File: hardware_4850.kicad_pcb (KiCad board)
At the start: 2 copper layers, 238 parts, among them J1 +, J10 Enable, J11 CAN_IN, J12 CAN_OUT, J13 Debug, J14 I2C, J2 Display, J3 A, J4 HALL, J5 B, J6 MOT_AUX, J7 C, J8 GND, J9 CRANK, P1 SWD, Q1 IPT015N10N5, Q2 IPT015N10N5, Q3 IPT015N10N5, Q4 IPT015N10N5, Q5 IPT015N10N5, Q6 IPT015N10N5, U1 1EDN7550B, U10 LM5008, U11 XC6206P332MR, U12 XC6206P332MR, U13 LMR12010X, U14 STM32G473VCTx, U15 SN65HVD230, U2 INA240A2PWR, U3 1EDN7550B, U4 1EDN7550B, U5 INA240A2PWR, U6 1EDN7550B, U7 1EDN7550B, U8 INA240A2PWR, U9 1EDN7550B, Y1 8MHz

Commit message: started the layout
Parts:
- added N1: Housing, footprints:HaiLong-Case, F.Cu at (50.0, 50.0)
- C15, C16, C3, C35, C36, C37, C38, C39, C4, C40, C41, C42, C43, C44, R17, R26, R8, U2, U5, U8: moved to B.Cu
- moved C44 253.2 mm to (87.5, 138.0), turned to 270 degrees
- moved C43 250.2 mm to (92.0, 138.0), turned to 270 degrees
- moved C10 249.1 mm to (55.4, 148.0)
- moved C11 249.1 mm to (46.0, 155.4)
- moved C12 249.1 mm to (31.9, 165.7)
- moved C5 249.1 mm to (51.7, 155.4)
- moved C6 249.1 mm to (43.6, 160.0)
- moved C7 249.1 mm to (61.1, 143.8)
- moved C8 249.1 mm to (38.0, 160.0)
- moved C9 249.1 mm to (37.5, 165.7)
- moved C40 246.9 mm to (105.5, 138.0), turned to 270 degrees
- moved C38 238.4 mm to (101.0, 133.0), turned to 90 degrees
- moved C47 237.2 mm to (11.7, 27.9)
- moved C48 237.2 mm to (5.95, 33.9)
- moved R29 237.2 mm to (14.5, 24.4)
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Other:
- board outline added: 100 x 55 mm
- board text added: "BATT Side"
- board text added: "Output Side"

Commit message: switched to old housing
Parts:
- removed J14: I2C, Connector_Wire:SolderWire-0.5sqmm_1x02_P4.6mm_D0.9mm_OD2.1mm
- added H1: MountingHole_Pad, MountingHole:MountingHole_3.2mm_M3_Pad_Via, F.Cu at (97.5, 94.5)
- added H2: MountingHole_Pad, MountingHole:MountingHole_3.2mm_M3_Pad_Via, F.Cu at (129.5, 94.5)
- added H3: MountingHole_Pad, MountingHole:MountingHole_3.2mm_M3_Pad_Via, F.Cu at (161.5, 94.5)
- C15, C16, C3, C35, C36, C37, C38, C39, C4, C40, C41, C42, C43, C44, R17, R26, R8, U2, U5, U8: moved to F.Cu
- J1, J3, J5, J7, J8: footprint Connector_Wire:SolderWire-2.5sqmm_1x01_D2.4mm_OD3.6mm -> footprints:8X8X8.4MM TERMINAL
- J10: footprint Connector_JST:JST_PH_S2B-PH-K_1x02_P2.00mm_Horizontal -> Connector_JST:JST_PH_B2B-PH-K_1x02_P2.00mm_Vertical
- J11, J12, J6, J9: footprint Connector_JST:JST_PH_S4B-PH-K_1x04_P2.00mm_Horizontal -> Connector_JST:JST_PH_B4B-PH-K_1x04_P2.00mm_Vertical
- J13: footprint Connector_USB:USB_Mini-B_Lumberg_2486_01_Horizontal -> Connector_USB:USB_Micro-B_Wuerth_614105150721_Vertical
- J2, J4: footprint Connector_JST:JST_PH_S5B-PH-K_1x05_P2.00mm_Horizontal -> Connector_JST:JST_PH_B5B-PH-K_1x05_P2.00mm_Vertical
- JP10, JP11, JP12, JP13, JP14, JP15, JP16, JP2, JP3, JP4, JP5, JP6, JP7, JP8, JP9: footprint Jumper:SolderJumper-2_P1.3mm_Bridged_RoundedPad1.0x1.5mm -> NetTie:NetTie-2_SMD_Pad0.5mm
- N1: footprint footprints:HaiLong-Case -> footprints:RND-455-00370
- moved C48 267.7 mm to (266.0, -29.6)
- moved C47 251.2 mm to (257.2, -25.0)
- moved U8 232.2 mm to (259.6, -28.5), turned to 0 degrees
- moved C16 228.1 mm to (249.2, -29.6)
- moved C15 217.5 mm to (240.5, -25.0)
- moved C32 187.0 mm to (249.2, -18.8)
- moved U5 183.3 mm to (242.9, -17.8), turned to 0 degrees
- moved C31 170.9 mm to (240.5, -14.3)
- moved U2 165.1 mm to (242.9, -28.5), turned to 0 degrees
- moved J1 133.0 mm to (175.5, 114.5), turned to 90 degrees
- moved U14 126.4 mm to (129.5, 66.5)
- moved R29 98.6 mm to (89.5, 88.5), turned to 90 degrees
- moved C12 97.3 mm to (117.0, 118.5), turned to 180 degrees
- moved C9 96.2 mm to (117.0, 111.5), turned to 180 degrees
- moved C8 86.6 mm to (112.0, 115.0)
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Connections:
- net /mcu/AIN_TEMP renamed /mcu/AIN_TEMP_A
- U14 pad 78: /mcu/I2C_SCL -> (no net)
- U14 pad 94: /mcu/I2C_SDA -> (no net)
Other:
- board size 100 x 55 mm -> 104 x 79 mm
- copper layers 2 -> 4
- board text removed: "BATT Side"
- board text removed: "Output Side"

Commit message: finished placing started layout
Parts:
- removed JP10: PBN+, NetTie:NetTie-2_SMD_Pad0.5mm
- removed JP12: PCN+, NetTie:NetTie-2_SMD_Pad0.5mm
- removed JP2: PA+, NetTie:NetTie-2_SMD_Pad0.5mm
- removed JP4: PB+, NetTie:NetTie-2_SMD_Pad0.5mm
- removed JP6: PC+, NetTie:NetTie-2_SMD_Pad0.5mm
- removed JP8: PAN+, NetTie:NetTie-2_SMD_Pad0.5mm
- added C92: 100n, Capacitor_SMD:C_0603_1608Metric, F.Cu at (132.6, 62.1)
- added C93: 100n, Capacitor_SMD:C_0603_1608Metric, F.Cu at (132.6, 68.2)
- added C94: 100n, Capacitor_SMD:C_0603_1608Metric, F.Cu at (109.1, 55.4)
- added C95: 100n, Capacitor_SMD:C_0603_1608Metric, F.Cu at (118.0, 55.4)
- added C96: 100n, Capacitor_SMD:C_0603_1608Metric, F.Cu at (106.2, 70.0)
- added R67: 10k, Resistor_SMD:R_0603_1608Metric, F.Cu at (112.1, 55.4)
- added R68: 1k, Resistor_SMD:R_0603_1608Metric, F.Cu at (132.6, 60.6)
- added R69: 33k, Resistor_SMD:R_0603_1608Metric, F.Cu at (140.7, 88.0)
- added R70: 10k, Resistor_SMD:R_0603_1608Metric, F.Cu at (132.6, 66.7)
- added R71: 1k, Resistor_SMD:R_0603_1608Metric, F.Cu at (110.6, 55.4)
- added R72: 33k, Resistor_SMD:R_0603_1608Metric, F.Cu at (107.8, 88.4)
- added R73: 10k, Resistor_SMD:R_0603_1608Metric, F.Cu at (119.5, 55.4)
- added R74: 1k, Resistor_SMD:R_0603_1608Metric, F.Cu at (106.2, 68.6)
- added TH2: NTC 10k, Resistor_SMD:R_0603_1608Metric, F.Cu at (134.0, 97.0)
- added TH3: NTC 10k, Resistor_SMD:R_0603_1608Metric, F.Cu at (166.5, 96.5)
- JP11, JP13, JP3, JP5, JP7, JP9: moved to B.Cu
- L2: value 4u7 -> 10u; footprint Inductor_SMD:L_1206_3216Metric -> Inductor_SMD:L_Taiyo-Yuden_NR-40xx
- R1: value 10k -> 33k
- R2: value 33k -> 1k
- R3: value 1k -> 33k
- moved J2 220.8 mm to (178.0, 87.5), turned to 90 degrees
- moved R3 204.7 mm to (173.2, 89.1), turned to 180 degrees
- moved R1 193.3 mm to (172.0, 86.0), turned to 180 degrees
- moved C48 187.8 mm to (102.5, 63.0), turned to 180 degrees
- moved U8 185.1 mm to (102.5, 69.4), turned to 90 degrees
- moved C47 178.7 mm to (102.5, 64.5), turned to 180 degrees
- moved R46 173.7 mm to (83.5, 89.2)
- moved J12 172.4 mm to (141.2, 72.0), turned to 0 degrees
- moved R47 167.7 mm to (83.5, 87.8)
- moved R48 161.8 mm to (83.5, 86.2)
- moved J11 161.6 mm to (141.2, 66.5), turned to 0 degrees
- moved D11 158.3 mm to (80.5, 87.8)
- moved JP13 156.2 mm to (116.4, 77.9), turned to 270 degrees
- moved C78 153.4 mm to (129.3, 74.4), turned to 270 degrees
- moved D10 150.3 mm to (80.5, 89.2)
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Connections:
- net Net-(C29-Pad2) renamed /phase_b/Phase-
- net Net-(C45-Pad2) renamed /phase_c/Phase-
- C1 pad 1: /mcu/AIN_TEMP_A -> /mcu/AIN_VDC
- C13 pad 2: Net-(C13-Pad2) -> /phase_a/Phase-
- C14 pad 2: Net-(C13-Pad2) -> /phase_a/Phase-
- C2 pad 1: /mcu/AIN_VDC -> /mcu/AIN_TEMP_A
- J3 pad 1: /phase_a/Phase -> Net-(J3-Pad1)
- J5 pad 1: /phase_b/Phase -> Net-(J5-Pad1)
- J7 pad 1: /phase_c/Phase -> Net-(J7-Pad1)
- Q1 pad 2: Net-(C13-Pad2) -> /phase_a/Phase-
- Q2 pad 3: Net-(C13-Pad2) -> /phase_a/Phase-
- R1 pad 1: /Interface/VREF -> +BATT
- R1 pad 2: /mcu/AIN_TEMP_A -> /mcu/AIN_VDC
- R17 pad 1: /phase_b/Phase -> /phase_b/Phase+
- R2 pad 1: +BATT -> /mcu/AIN_VDC
- R2 pad 2: /mcu/AIN_VDC -> GNDA
- R26 pad 1: /phase_c/Phase -> /phase_c/Phase+
- R3 pad 1: /mcu/AIN_VDC -> /phase_a/Phase-
- R3 pad 2: GNDA -> /mcu/AIN_VA
- R51 pad 1: +5V -> +3V3
- R52 pad 1: +5V -> +3V3
- R53 pad 1: +5V -> +3V3
- R54 pad 1: +5V -> +3V3
- R61 pad 1: +5V -> +3V3
- R8 pad 1: /phase_a/Phase -> /phase_a/Phase+
- R8 pad 2: Net-(C13-Pad2) -> /phase_a/Phase-
- U1 pad 2: Net-(C13-Pad2) -> /phase_a/Phase-
- U14 pad 17: (no net) -> /mcu/AIN_TEMP_B
- U14 pad 20: (no net) -> /mcu/AIN_VA
- U14 pad 38: (no net) -> /mcu/AIN_TEMP_C
- U14 pad 45: (no net) -> /mcu/AIN_VB
- U14 pad 61: (no net) -> /mcu/AIN_VC
- U14 pad 65: Net-(JP2-Pad1) -> /mcu/PWM_A+
- U14 pad 66: Net-(JP4-Pad1) -> /mcu/PWM_B+
- U14 pad 67: Net-(JP6-Pad1) -> /mcu/PWM_C+
- U14 pad 79: Net-(JP8-Pad1) -> /mcu/PWM_AN+
- U14 pad 80: Net-(JP10-Pad1) -> /mcu/PWM_BN+
- U14 pad 81: Net-(JP12-Pad1) -> /mcu/PWM_CN+
- U2 pad 2: /phase_a/Phase -> /phase_a/Phase+
- U2 pad 3: Net-(C13-Pad2) -> /phase_a/Phase-
- U5 pad 2: /phase_b/Phase -> /phase_b/Phase+
- U8 pad 2: /phase_c/Phase -> /phase_c/Phase+
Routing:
- net GNDPWR: track 0.00 -> 183.8 mm, vias 0 -> 6
- net /phase_b/Phase-: track 0.00 -> 129.7 mm, vias 0 -> 2
- net /phase_b/Phase+: track 0.00 -> 108.4 mm, vias 0 -> 2
- net /phase_a/Phase-: track 0.00 -> 94.0 mm, vias 0 -> 2
- net /mcu/PWM_A+: track 0.00 -> 86.1 mm, vias 0 -> 2
- net /mcu/PWM_A-: track 0.00 -> 84.4 mm, vias 0 -> 1
- net /phase_c/Phase-: track 0.00 -> 79.5 mm, vias 0 -> 2
- net /phase_a/Phase+: track 0.00 -> 77.5 mm, vias 0 -> 2
- net /mcu/PWM_B+: track 0.00 -> 60.3 mm, vias 0 -> 2
- net /phase_c/Phase+: track 0.00 -> 60.1 mm, vias 0 -> 2
- net /mcu/PWM_B-: track 0.00 -> 56.6 mm, vias 0 -> 1
- net /mcu/PWM_AN-: track 0.00 -> 55.4 mm, vias 0 -> 1
- net /mcu/PWM_AN+: track 0.00 -> 52.5 mm, vias 0 -> 2
- net GNDA: track 0.00 -> 45.9 mm
- net /mcu/PWM_C+: track 0.00 -> 37.6 mm, vias 0 -> 2
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- added copper zone on VCC, net +3V3
- added copper zone on F.Cu, net +BATT
- added copper zone on VCC, net +BATT
- added copper zone on F.Cu, net /phase_a/Phase+
- added copper zone on F.Cu, net /phase_a/Phase-
- added copper zone on F.Cu, net /phase_b/Phase+
- added copper zone on F.Cu, net /phase_b/Phase-
- added copper zone on F.Cu, net /phase_c/Phase+
- added copper zone on F.Cu, net /phase_c/Phase-
- added copper zone on GND, net GNDD
- added copper zone on F.Cu, net GNDPWR
- added copper zone on GND, net GNDPWR
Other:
- net class Default: clearance 0.2 -> 0.127; trace_width 0.25 -> 0.2; via_dia 0.8 -> 0.4; via_drill 0.4 -> 0.2
- rule trace_clearance: 0.2 -> 0.127
- rule trace_min: 0.2 -> 0.127
- rule via_min_drill: 0.3 -> 0.2

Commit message: 26 routes to go
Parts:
- moved J9 65.5 mm to (147.9, 72.2), turned to 90 degrees
- moved R33 61.0 mm to (112.1, 82.7), turned to 270 degrees
- moved R64 59.1 mm to (143.6, 66.6)
- moved D6 58.8 mm to (112.1, 85.7), turned to 90 degrees
- moved R61 58.6 mm to (144.3, 70.9), turned to 90 degrees
- moved R65 58.3 mm to (143.6, 68.1)
- moved R63 55.6 mm to (142.8, 70.9), turned to 270 degrees
- moved J4 54.5 mm to (136.1, 71.6), turned to 90 degrees
- moved D9 50.1 mm to (106.2, 85.7), turned to 90 degrees
- moved J6 50.1 mm to (146.8, 53.9), turned to 270 degrees
- moved R38 48.6 mm to (106.2, 82.7), turned to 90 degrees
- moved R51 45.3 mm to (131.5, 70.8)
- moved R53 45.0 mm to (131.5, 63.3), turned to 0 degrees
- moved R56 44.8 mm to (131.5, 69.3)
- moved R58 44.7 mm to (131.5, 64.8), turned to 0 degrees
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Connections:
- J3 pad 1: Net-(J3-Pad1) -> /phase_a/Phase+
- J5 pad 1: Net-(J5-Pad1) -> /phase_b/Phase+
- J7 pad 1: Net-(J7-Pad1) -> /phase_c/Phase+
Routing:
- net /phase_b/Phase+: track 108.4 -> 0.00 mm, vias 2 -> 0
- net /phase_b/Phase-: track 129.7 -> 21.4 mm, vias 2 -> 0
- net GNDA: track 45.9 -> 151.7 mm, vias 0 -> 28
- net /mcu/DISP_TX: track 0.00 -> 91.2 mm
- net /mcu/DISP_RX: track 0.00 -> 86.1 mm
- net /mcu/PWM_A+: track 86.1 -> 0.00 mm, vias 2 -> 0
- net /mcu/PWM_A-: track 84.4 -> 0.00 mm, vias 1 -> 0
- net /mcu/AIN_CRK_TORQ: track 7.63 -> 87.6 mm, vias 0 -> 2
- net /phase_a/Phase+: track 77.5 -> 0.00 mm, vias 2 -> 0
- net /phase_a/Phase-: track 94.0 -> 19.1 mm, vias 2 -> 0
- net +5V: track 0.00 -> 68.0 mm, vias 0 -> 4
- net /mcu/PWM_B+: track 60.3 -> 0.00 mm, vias 2 -> 0
- net /mcu/PWM_B-: track 56.6 -> 0.00 mm, vias 1 -> 0
- net /mcu/AIN_TEMP_A: track 8.26 -> 64.2 mm
- net /mcu/PWM_AN-: track 55.4 -> 0.00 mm, vias 1 -> 0
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- added copper zone on F.Cu, net +12V
- added copper zone on VCC, net +12V
- added copper zone on B.Cu, net +3.3VADC
- added copper zone on F.Cu, net +5V
- added copper zone on VCC, net /Interface/VREF
- added copper zone on F.Cu, net /power_supply/DCDC_VIN
- added copper zone on GND, net GNDA
- added copper zone on F.Cu, net GNDD
- added copper zone on F.Cu, net Net-(C51-Pad1)
- added copper zone on F.Cu, net Net-(C52-Pad1)
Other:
- net class Default: trace_width 0.2 -> 0.127

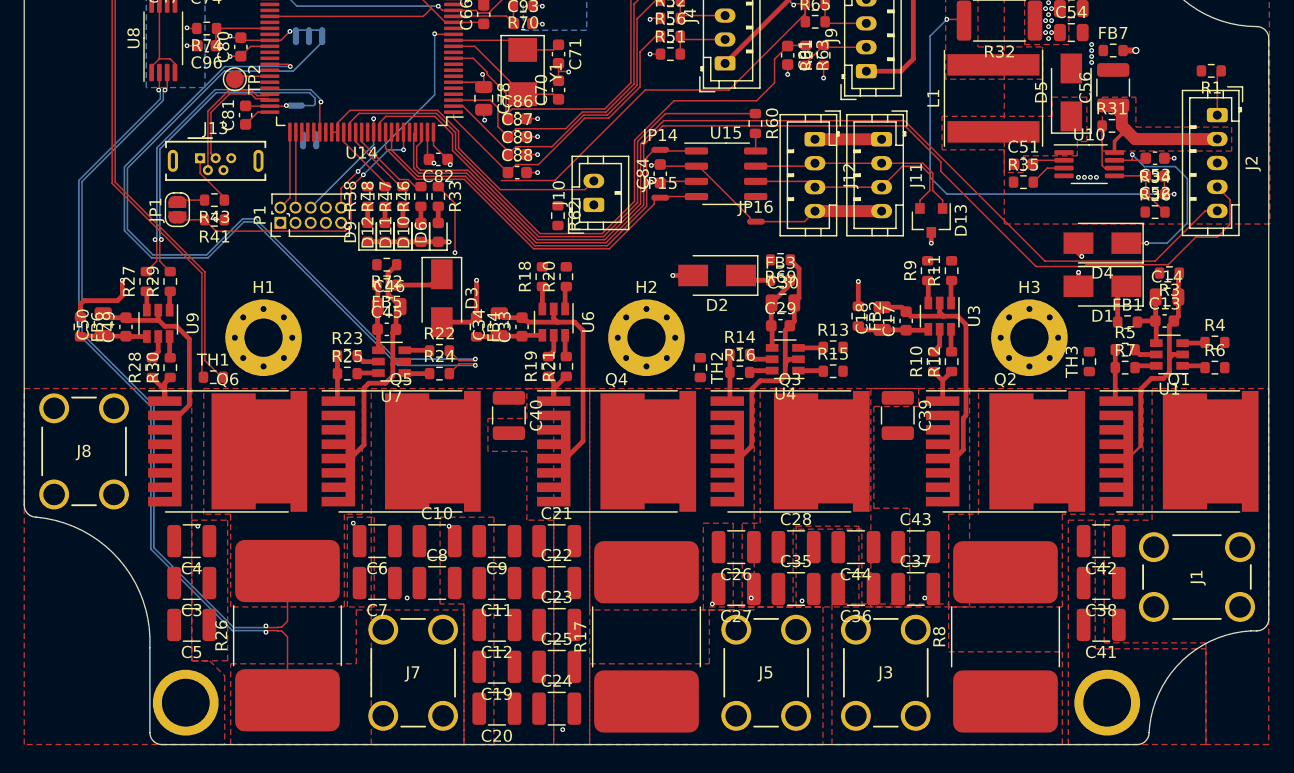
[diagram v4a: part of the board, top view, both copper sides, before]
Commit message: adding vias
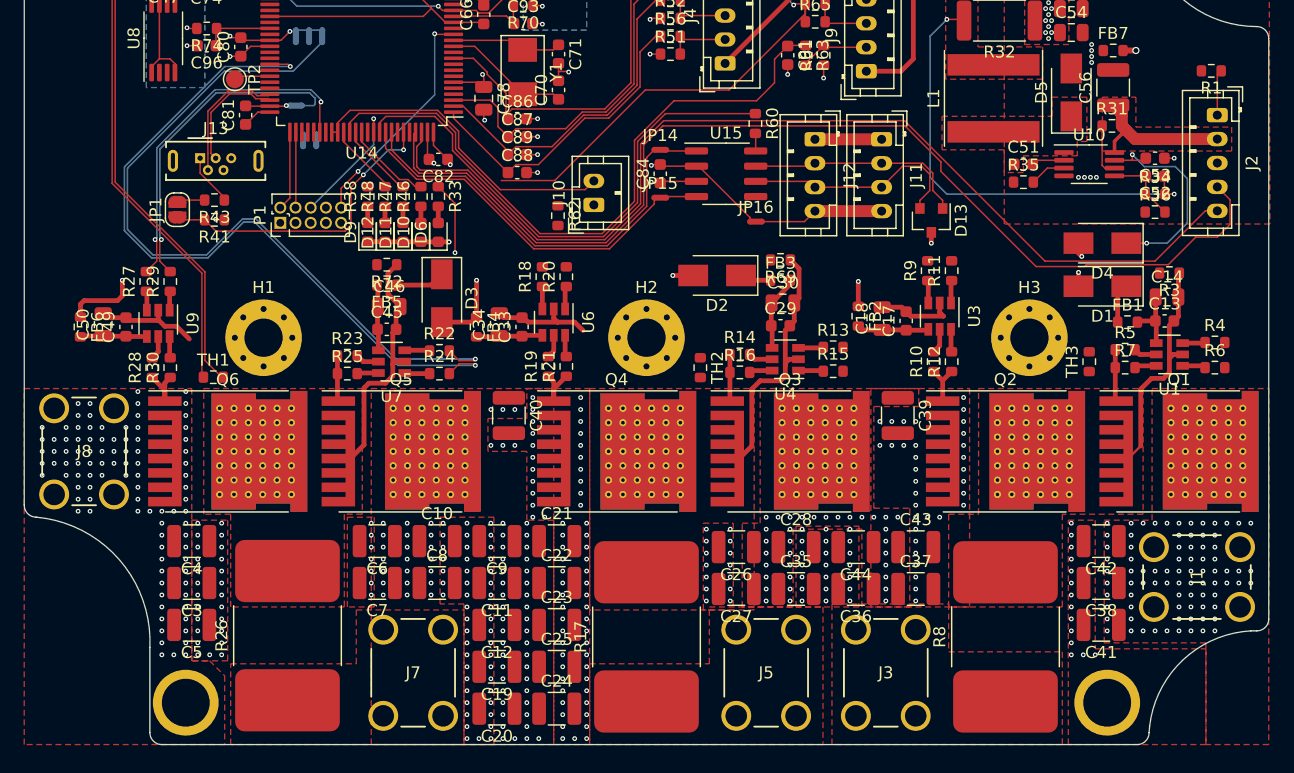
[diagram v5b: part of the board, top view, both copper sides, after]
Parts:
- Q1, Q2, Q3, Q4, Q5, Q6: footprint Package_TO_SOT_SMD:Infineon_PG-HSOF-8-1 -> Package_TO_SOT_SMD:Infineon_PG-HSOF-8-1_ThermalVias
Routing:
- net /phase_c/Phase+: track 65.1 -> 0.00 mm, vias 2 -> 0
- net /phase_c/Phase-: track 84.2 -> 20.6 mm, vias 2 -> 0
- net GNDPWR: track 190.8 -> 158.7 mm, vias 7 -> 296
- net +BATT: vias 3 -> 203
